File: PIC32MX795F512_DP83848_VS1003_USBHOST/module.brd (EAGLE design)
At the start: 109.9 x 68.6 mm, 114 parts, among them IC1 IC_USBLC6-2, IC2 LM1117IMPX-3.3, IC3 PIC32MX795F512, IC4 DP83848, IC5 LM1117MPX-2.5, U1 USD-SOCKETUSD, U2 VS1003, X2 CRYSTALS-NOGND-CFPX-217, X3 KUSBVX, Y3 CRYSTAL-GROUNDEDSMD-5X3.2

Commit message: Some updates
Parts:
- added C1: (no value), rcl:C0402
- added R14: (no value), rcl:R0402
- R12: value 0R -> (none)
- moved R12 25.9 mm to (41.4, 25.1)
- moved C5 12.7 mm to (38.9, 4.95), turned to 180 degrees
- moved C27 3.74 mm to (43.1, 11.0), turned to 0 degrees
- moved IC1 3.18 mm to (45.7, 16.7)
- moved X3 3.17 mm to (45.7, 12.7)
- moved C7 1.67 mm to (40.5, 33.4), turned to 270 degrees
- moved C9 1.28 mm to (41.6, 43.4), turned to 90 degrees
- moved JP3 0.61 mm to (36.6, 26.1)
- moved C8 0.25 mm to (36.9, 38.6)
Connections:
- removed net CE1: R12.2, R13.1, U$2.1
- new net SDA1A: IC3.52, R14.1, SV1.2
- net 3V: now also C1.1, R12.2, R14.2
- net FLASH_CS: now also IC3.38, R13.1, U$2.1; no longer IC3.52, R12.1
- net GND: now also C1.2
- net SCL1A: now also R12.1
- net SD_CS: now also IC3.44; no longer IC3.38
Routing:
- net SDA1A: track 0.00 -> 48.4 mm
- net SCL1A: track 14.9 -> 49.0 mm
- net 3V: track 559.5 -> 570.8 mm
- net FLASH_CS: track 41.5 -> 49.3 mm
- net CE1: track 4.89 -> 0.00 mm
- net D_N: track 20.3 -> 17.2 mm
- net D_P: track 20.3 -> 17.1 mm
- net GND: track 75.2 -> 78.2 mm, vias 42 -> 43
- net SD_CS: track 45.5 -> 43.3 mm
- net VBUS: track 188.9 -> 191.0 mm, vias 2 -> 4
- net AN_3V: track 9.83 -> 8.38 mm
- net SD_PRESENT: track 47.4 -> 46.3 mm
- net MOSI: track 44.3 -> 43.4 mm
- net TXD: track 12.3 -> 12.9 mm
- net RXD: track 18.7 -> 19.4 mm
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
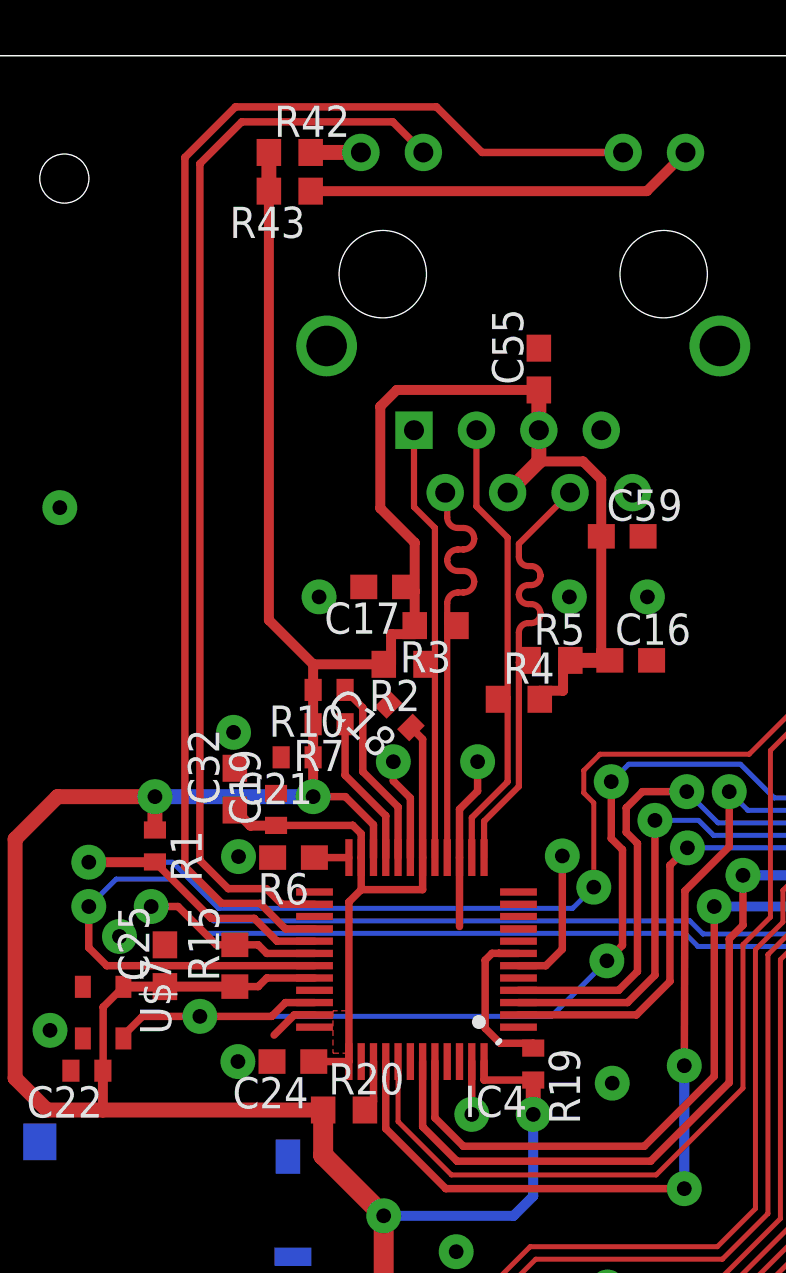
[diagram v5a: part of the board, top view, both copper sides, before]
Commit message: Ethernet AVDD filtering
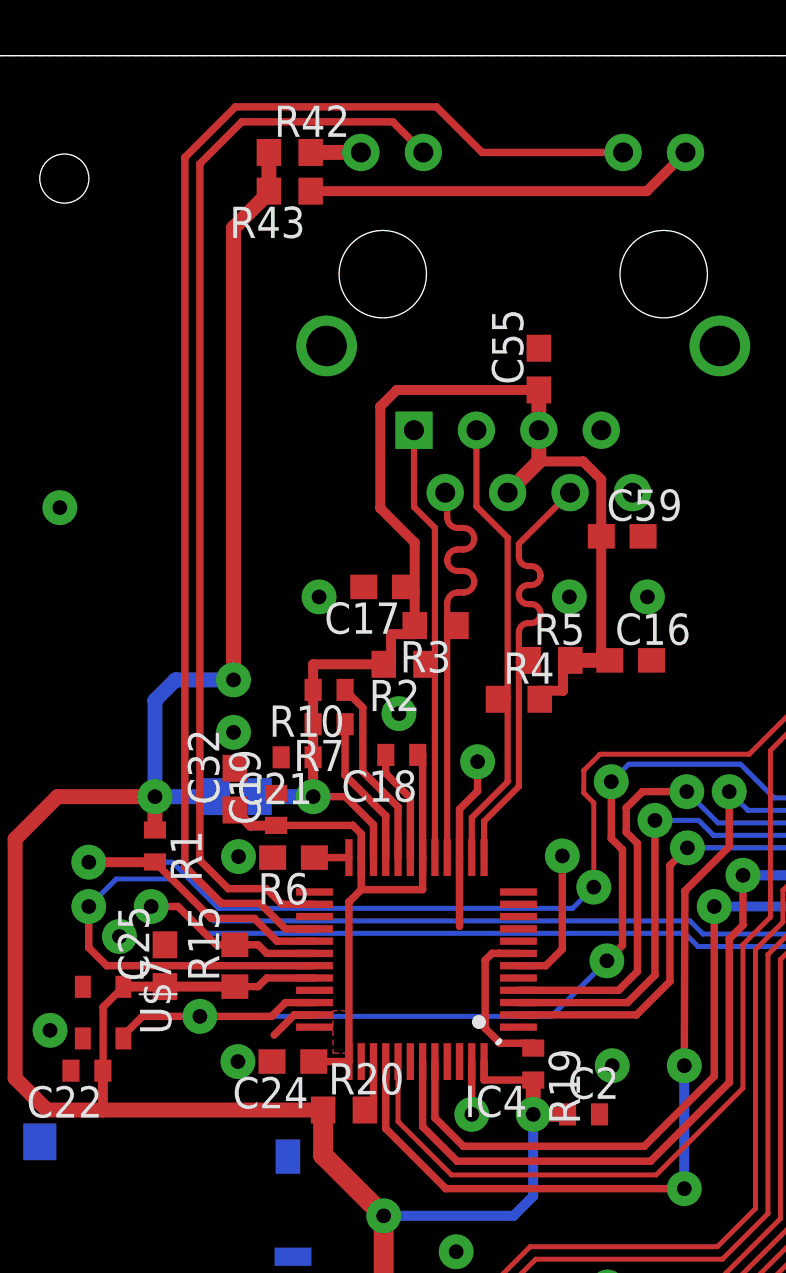
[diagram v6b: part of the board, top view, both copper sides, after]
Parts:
- added C2: (no value), rcl:C0402
- added L3: (no value), dp_devices:FB805
- moved C18 1.58 mm to (18.7, 40.1), turned to 180 degrees
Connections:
- new net A3V: C16.1, C17.1, C21.1, C55.1, C59.1, IC4.22, L3.2, R10.2, R2.2, R3.2, R4.2, R5.2, R7.2, RJ1.P4, RJ1.P5
- net 3V: now also C2.1, L3.1; no longer C16.1, C17.1, C21.1, C55.1, C59.1, IC4.22, R10.2, R2.2, R3.2, R4.2, R5.2, R7.2, RJ1.P4, RJ1.P5
- net GND: now also C2.2
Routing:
- net A3V: track 0.00 -> 53.6 mm, vias 0 -> 1
- net 3V: track 570.8 -> 523.3 mm
- net REG_OUT: track 25.8 -> 24.6 mm
